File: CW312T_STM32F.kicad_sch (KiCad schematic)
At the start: 24 parts, among them J1 HDR_6_2.54, P1 PCIEx4 EDGE CONNECTOR, U1 STM32F100RBT6B

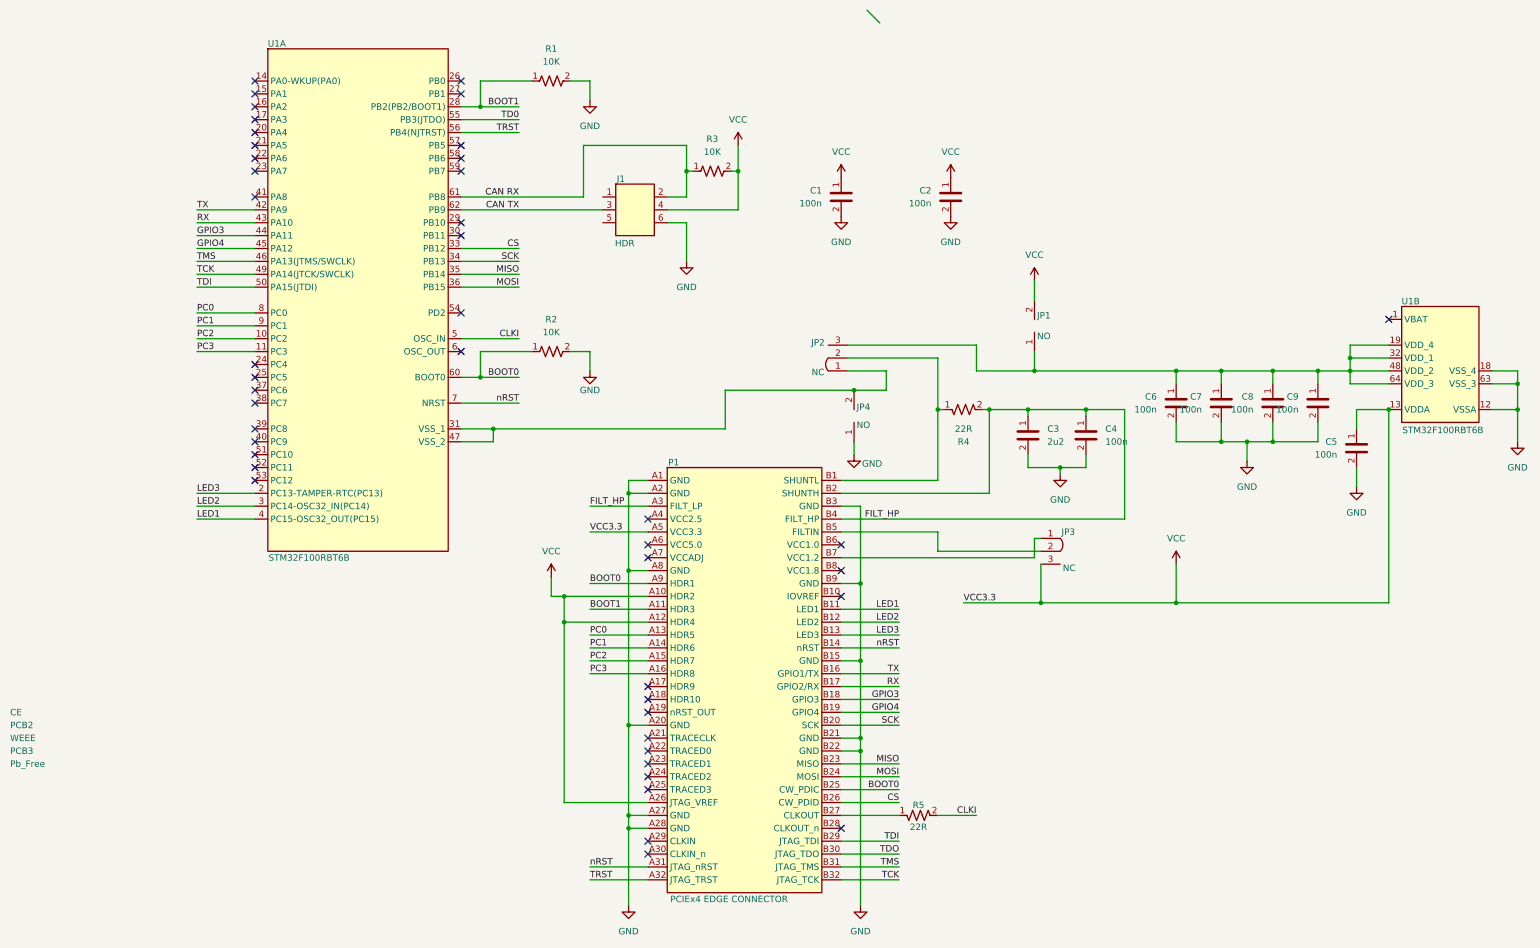
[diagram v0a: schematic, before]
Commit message: updated design - fixed connections, got rid of visible pin numbers on passives, updated silkscreen
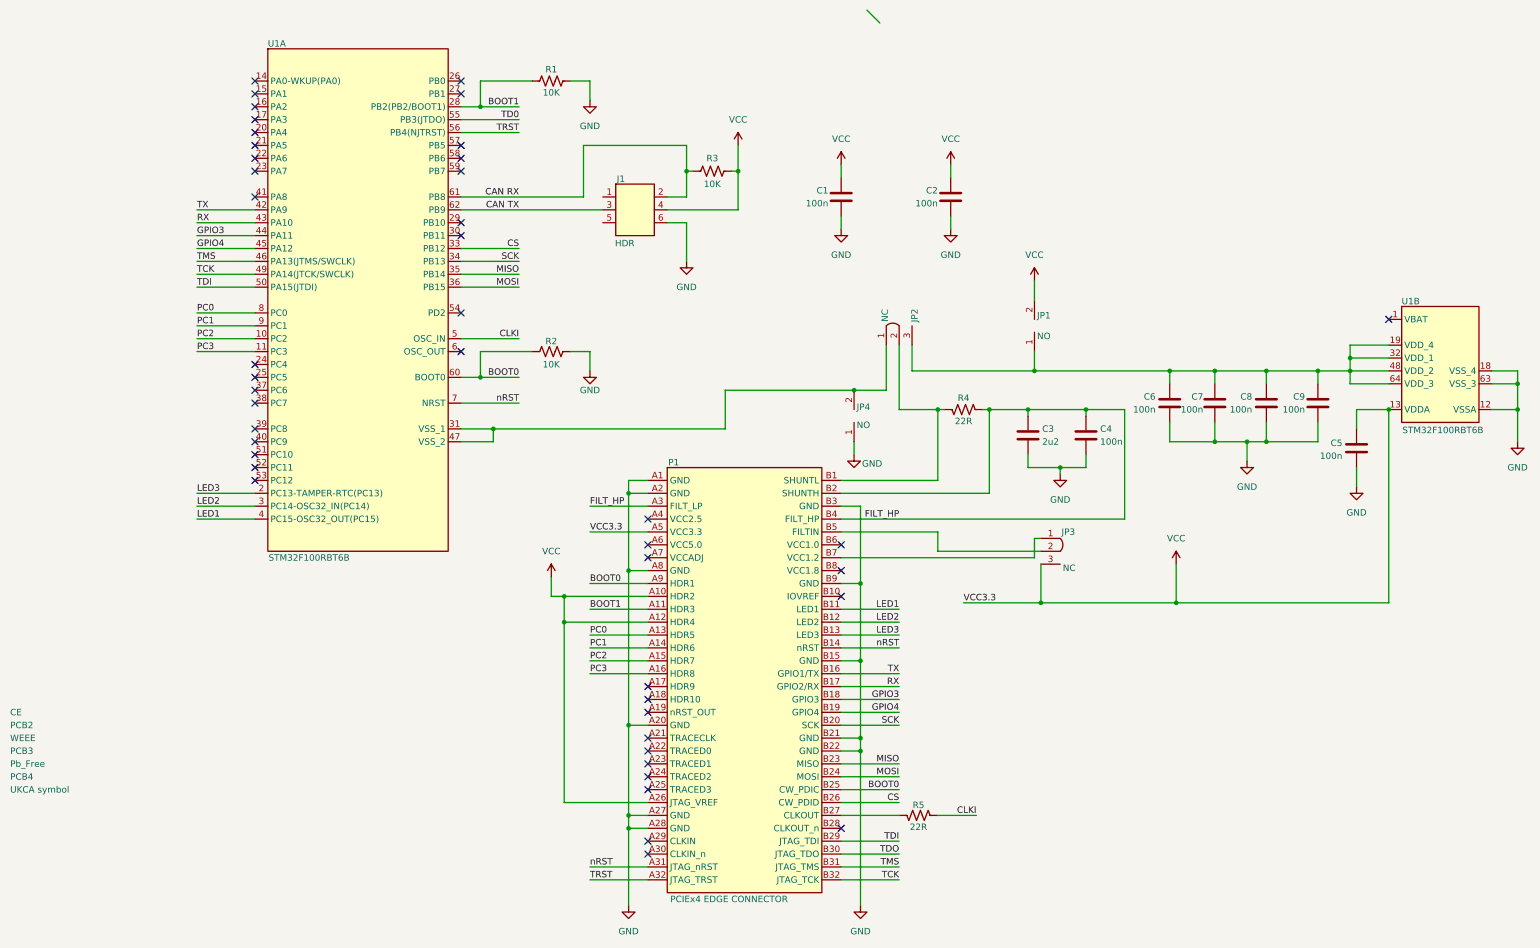
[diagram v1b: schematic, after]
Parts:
- added PCB4: UKCA symbol, Silkscrren_Symbols:UKCA-Logo_8x8mm_SilkScreen, symbol Silkscreen_Symbols:UKCA
- PCB2: footprint Silkscrren_Symbols:WEEE-Logo_8.4x12mm_SilkScreen -> Silkscrren_Symbols:WEEE-Logo_5.6x8mm_SilkScreen
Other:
- moved on the sheet: JP2
